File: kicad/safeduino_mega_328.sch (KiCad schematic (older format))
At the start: 75 parts, among them X1 USB

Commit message: Заменил FTDI на Atmega16u2.
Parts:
- removed DD2: FT232RL, symbol FT232RL
- removed DD3: ADUM1201, symbol ADUM1201
- removed XSJG1: ~, ~, symbol PIN_M_4
- added C1: 22п, symbol CAPITORS
- added C10, C8, C9: 0.1мк, symbol CAPITORS
- added DD2: ATMEGA16U2-MU, ~, symbol ATMEGA16U2-MU
- added DD3: ADUM1301, ~, symbol ADUM1301
- added R10, R12, R13: 10к, symbol RESISTOR
- added R11: 1M, symbol RESISTOR
- added R14, R15: 0, symbol RESISTOR
- added R16: 1М, symbol RESISTOR
- added R9: 1к, symbol RESISTOR
- added VD5: BAS216, ~, symbol DIODE
- added XP1: PLD-6, ~, symbol PIN_M_6
- added Z2: 16МГц, symbol QUARTZ_RESONATOR
- C3: value 0.1мк -> 22п
- C5: value 0.1мк -> 1мк
- R3: value 47 -> 22
- R4: value 1к -> 22
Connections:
- net labels added: D+, D-, MISO2, MOSI2, PE0, PE1, RESET2, RESET_16U2, RXI, SCK2, TXI
- net labels removed: CTS, DCD, DSR, RI
- wire segments 237 -> 326
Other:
- note removed: "MISO"
- note removed: "MOSI"
- note removed: "RESET"
- note removed: "SCK"
- moved on the sheet: C13, C14, C15, C16, C17, C18, C2, C21, C23, C6, C7, DA1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

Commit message: Начал переразводить печатную плату.
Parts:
- R14: value 0 -> 1к
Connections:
- wire segments 326 -> 280
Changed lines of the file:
@@
 	13050 9450 13300 9450
 Wire Wire Line
-	4150 3400 4150 4000
-Wire Wire Line
-	4150 4000 4150 4150
+	4150 3400 4150 4150
 Wire Wire Line
 	4150 3400 3700 3400
@@
 	2750 4600 2750 4400
 Wire Wire Line
-	2750 4600 3550 4600
-Wire Wire Line
-	3550 4600 4150 4600
-Wire Wire Line
-	4150 4600 4900 4600
-Wire Wire Line
-	4900 4600 5500 4600
+	2750 4600 5500 4600
 Wire Wire Line
 	1650 1850 1650 1600
@@
 Connection ~ 4150 4000
 Wire Wire Line
-	2200 4000 2750 4000
-Wire Wire Line
-	2750 4000 3100 4000
+	2200 4000 3100 4000
 Wire Wire Line
 	4150 4600 4150 4400
@@
 Connection ~ 12200 2450
 Wire Wire Line
-	10650 2450 12200 2450
-Wire Wire Line
-	12200 2450 12650 2450
+	10650 2450 12650 2450
 Connection ~ 11200 2650
 Wire Wire Line
-	10650 2650 11200 2650
-Wire Wire Line
-	11200 2650 11650 2650
+	10650 2650 11650 2650
 Wire Wire Line
 	11200 3000 11200 3250
@@
 Connection ~ 9400 3950
 Wire Wire Line
-	9250 3950 9400 3950
-Wire Wire Line
-	9400 3950 9650 3950
+	9250 3950 9650 3950
 Wire Wire Line
 	8550 4150 8400 4150
@@
 	14450 1250 14900 1250
 Wire Wire Line
-	14450 1350 14800 1350
-Wire Wire Line
-	14800 1350 14900 1350
+	14450 1350 14900 1350
 Wire Wire Line
 	14450 1150 14900 1150
@@
 	6700 2750 7000 2750
 Wire Wire Line
-	6700 2750 6700 2950
-Wire Wire Line
-	6700 2950 6700 3500
-Wire Wire Line
-	6700 3500 6700 3600
+	6700 2750 6700 3600
 Connection ~ 6450 3950
 Wire Wire Line
@@
 	6600 3500 6700 3500
 Wire Wire Line
-	10750 2850 10750 2950
-Wire Wire Line
-	10750 2950 10750 3050
+	10750 2850 10750 3050
 Wire Wire Line
 	10750 2850 10650 2850
@@
 	6100 2450 7000 2450
 Wire Wire Line
-	2450 2300 2950 2300
-Wire Wire Line
-	2950 2300 3050 2300
-Wire Wire Line
-	1550 7450 1650 7450
-Wire Wire Line
-	1650 7450 2050 7450
+	2450 2300 3050 2300
+Wire Wire Line
+	1550 7450 2050 7450
 Connection ~ 1650 7450
 Wire Wire Line
@@
 	6200 3950 6200 3850
 Wire Wire Line
-	6200 3950 6450 3950
-Wire Wire Line
-	6450 3950 6700 3950
+	6200 3950 6700 3950
 Wire Wire Line
 	6700 3950 6700 3850
@@
 	6200 2650 7000 2650
 Wire Wire Line
-	6200 2650 6200 2950
-Wire Wire Line
-	6200 2950 6200 3500
-Wire Wire Line
-	6200 3500 6200 3600
+	6200 2650 6200 3600
 Wire Wire Line
 	7000 1850 6100 1850
@@
 	6100 2050 7000 2050
 Wire Wire Line
-	8100 3950 8400 3950
-Wire Wire Line
-	8400 3950 8550 3950
+	8100 3950 8550 3950
 Connection ~ 8400 3950
 Wire Wire Line
@@
 	4700 2400 5150 2400
 Wire Wire Line
-	10650 3050 10750 3050
-Wire Wire Line
-	10750 3050 11050 3050
+	10650 3050 11050 3050
 Connection ~ 10750 3050
 Wire Wire Line
@@
 	12200 3400 12200 3650
 Wire Wire Line
-	10650 2550 11700 2550
-Wire Wire Line
-	11700 2550 12150 2550
+	10650 2550 12150 2550
 Connection ~ 11700 2550
 Wire Wire Line
@@
 	12300 6800 13100 6800
 Wire Wire Line
-	4000 4000 4150 4000
-Wire Wire Line
-	4150 4000 4900 4000
-Wire Wire Line
-	4900 4000 5500 4000
+	4000 4000 5500 4000
 Connection ~ 4900 4000
 Wire Wire Line
@@
 	1950 2500 1450 2500
 Wire Wire Line
-	2750 3400 2750 4000
-Wire Wire Line
-	2750 4000 2750 4150
+	2750 3400 2750 4150
 Wire Wire Line
 	2750 3400 3400 3400
@@
 	3400 8800 3700 8800
 Wire Wire Line
-	3400 8800 3400 9000
-Wire Wire Line
-	3400 9000 3400 9550
-Wire Wire Line
-	3400 9550 3400 9650
+	3400 8800 3400 9650
 Connection ~ 3150 10000
 Wire Wire Line
-	3150 10250 3150 10000
+	3150 10450 3150 10000
 Wire Wire Line
 	3300 9550 3400 9550
@@
 	2900 10000 2900 9900
 Wire Wire Line
-	2900 10000 3150 10000
-Wire Wire Line
-	3150 10000 3400 10000
+	2900 10000 3400 10000
 Wire Wire Line
 	3400 10000 3400 9900
@@
 	2900 8700 3700 8700
 Wire Wire Line
-	2900 8700 2900 9000
-Wire Wire Line
-	2900 9000 2900 9550
-Wire Wire Line
-	2900 9550 2900 9650
+	2900 8700 2900 9650
 Wire Wire Line
 	3400 9000 3275 9000
@@
 	1    0    0    -1
 $EndComp
-Text Label 3150 10250 1    60   ~ 0
-GND
 $Comp
 L CAPITORS C3
@@
 	2400 9550 2400 9450
 Wire Wire Line
-	1800 9550 2100 9550
-Wire Wire Line
-	2100 9550 2400 9550
+	1800 9550 2400 9550
 Wire Wire Line
 	1800 9550 1800 9450
@@
 GND_USB
 Wire Wire Line
-	7650 8200 9050 8200
-Wire Wire Line
-	9050 8200 9450 8200
+	7650 8200 9450 8200
 Text Label 9450 8200 2    60   ~ 0
 5V_USB
@@
 	7650 8600 7750 8600
 Wire Wire Line
-	7750 8600 7750 8700
-Wire Wire Line
-	7750 8700 7750 8850
+	7750 8600 7750 8850
 Wire Wire Line
 	7750 8700 7650 8700
 Wire Wire Line
-	7750 8850 7950 8850
-Wire Wire Line
-	7950 8850 8500 8850
-Wire Wire Line
-	8500 8850 9050 8850
+	7750 8850 9050 8850
 Wire Wire Line
 	7950 8850 7950 8750
 Connection ~ 7750 8700
 Wire Wire Line
-	7650 8400 7950 8400
-Wire Wire Line
-	7950 8400 8350 8400
+	7650 8400 8350 8400
 Wire Wire Line
 	7950 8400 7950 8500
@@
 $EndComp
 Wire Wire Line
-	7650 8300 8500 8300
-Wire Wire Line
-	8500 8300 8900 8300
+	7650 8300 8900 8300
 Wire Wire Line
 	8500 8300 8500 8500
@@
 Connection ~ 7950 8400
 Wire Wire Line
-	8500 8750 8500 8850
-Wire Wire Line
-	8500 8850 8500 9300
+	8500 8750 8500 9300
 Connection ~ 7950 8850
 Wire Wire Line
@@
 	1450 5500 2150 5500
 Wire Wire Line
-	1450 5600 2600 5600
-Wire Wire Line
-	2600 5600 2750 5600
+	1450 5600 2750 5600
 Wire Wire Line
 	2050 5700 1450 5700
@@
 	2800 5900 2600 5900
 Wire Wire Line
-	2600 5600 2600 5900
-Wire Wire Line
-	2600 5900 2600 6250
+	2600 5600 2600 6250
 Connection ~ 2600 5600
 Wire Wire Line
-	3050 5600 3200 5600
-Wire Wire Line
-	3200 5600 3600 5600
+	3050 5600 3600 5600
 Wire Wire Line
 	3200 5600 3200 5900
@@
 	9900 6300 9900 6600
 Wire Wire Line
-	9500 6600 9900 6600
-Wire Wire Line
-	9900 6600 10000 6600
+	9500 6600 10000 6600
 Connection ~ 9900 6600
 Text Label 9500 6600 0    60   ~ 0
@@
 	9800 7550 9800 7200
 Wire Wire Line
-	9350 7200 9800 7200
-Wire Wire Line
-	9800 7200 10000 7200
+	9350 7200 10000 7200
 Wire Wire Line
 	10000 7300 9900 7300
@@
 	9900 7300 9900 7400
 Wire Wire Line
-	9350 7400 9900 7400
-Wire Wire Line
-	9900 7400 10000 7400
+	9350 7400 10000 7400
 Text Label 9350 7400 0    60   ~ 0
 GND_USB
@@
 	11900 7300 11900 7400
 Wire Wire Line
-	11800 7400 11900 7400
-Wire Wire Line
-	11900 7400 12550 7400
+	11800 7400 12550 7400
 Connection ~ 11900 7400
 Text Label 12550 7400 2    60   ~ 0
@@
 	12000 7550 12000 7200
 Wire Wire Line
-	11800 7200 12000 7200
-Wire Wire Line
-	12000 7200 12550 7200
+	11800 7200 12550 7200
 Connection ~ 12000 7200
 $Comp
@@
 P 11900 5850
 F 0 "R14" V 12100 6050 71  0000 C CNN
-F 1 "0" V 11950 6050 71  0000 C CNN
+F 1 "1к" V 11950 6050 71  0000 C CNN
 F 2 "" H 11900 5850 60  0001 C CNN
 F 3 "" H 11900 5850 60  0001 C CNN
 	1    11900 5850
-	0    1    -1   0
+	0    -1   -1   0
 $EndComp
 Wire Wire Line
@@
 GND
 Wire Wire Line
-	11900 5850 11900 6000
-Wire Wire Line
-	11900 6000 11900 6150
+	11900 5850 11900 6150
 Wire Wire Line
 	11900 6000 12350 6000
@@
 $EndComp
 Wire Wire Line
-	12600 6000 13000 6000
-Wire Wire Line
-	13000 6000 13400 6000
+	12600 6000 13400 6000
 Wire Wire Line
 	13000 6000 13000 5850
@@
 RESET
 Connection ~ 13000 6000
+Text Label 3150 10450 1    60   ~ 0
+GND_USB
 $EndSCHEMATC

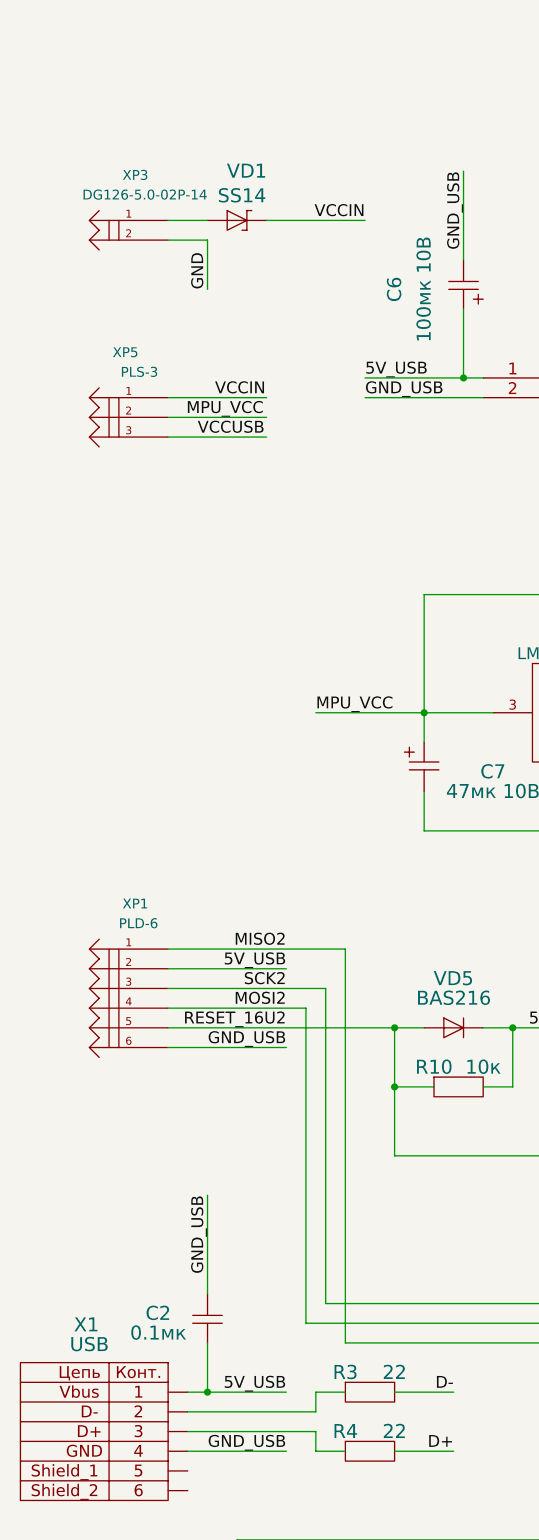
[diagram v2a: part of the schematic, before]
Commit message: Добавил самовостанавливающиеся предохренители на 0.5А.
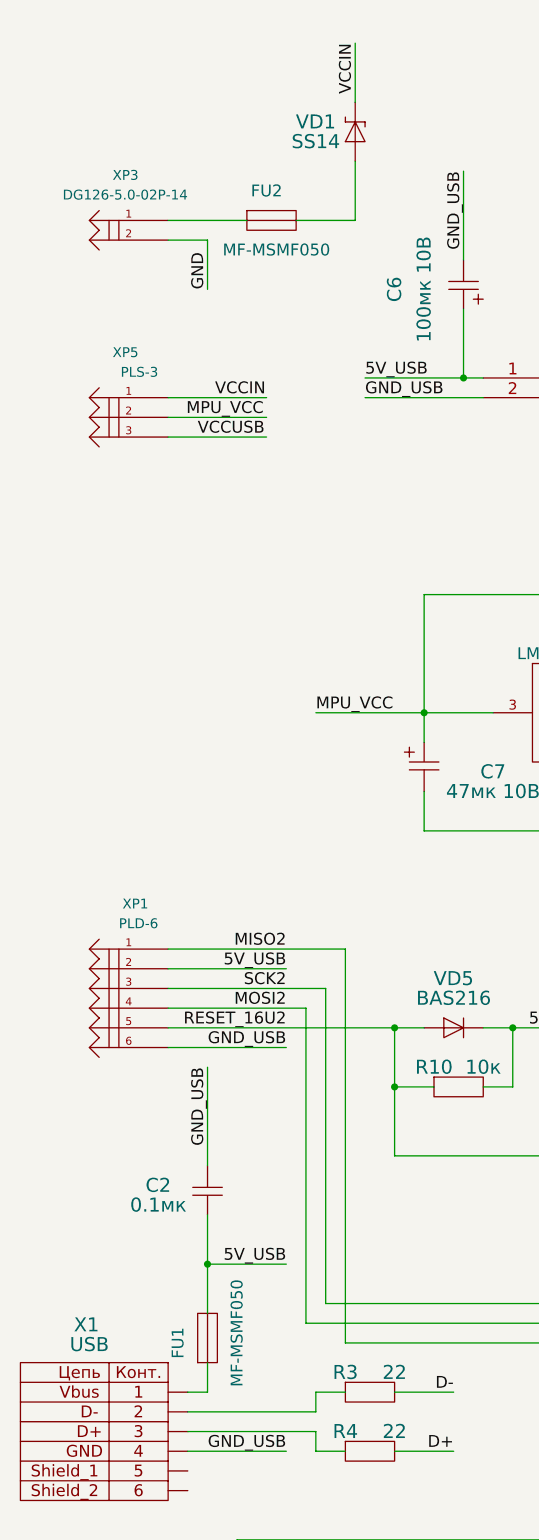
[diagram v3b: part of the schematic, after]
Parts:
- added FU1, FU2: MF-MSMF050, ~, symbol PROTECTOR
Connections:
- wire segments 280 -> 284
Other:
- moved on the sheet: C2, VD1
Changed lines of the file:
@@
 Sheet 1 1
 Title "SafeDuino MEGA 328"
-Date "19 feb 2016"
+Date "24 feb 2016"
 Rev "1.02"
 Comp ""
@@
 	13450 2250 13000 2250
 Wire Wire Line
-	1950 1500 2450 1500
-Wire Wire Line
 	1950 2600 1450 2600
 Wire Wire Line
@@
 	2450 2300 3050 2300
 Wire Wire Line
-	1550 7450 2050 7450
-Connection ~ 1650 7450
-Wire Wire Line
-	1650 7200 1650 7450
-Wire Wire Line
-	1650 6950 1650 6450
+	1650 6800 2050 6800
+Connection ~ 1650 6800
+Wire Wire Line
+	1650 6550 1650 7050
+Wire Wire Line
+	1650 6300 1650 5800
 Wire Wire Line
 	12000 8050 12000 7800
@@
 	14900 1550 14450 1550
 Wire Wire Line
-	1450 1500 1650 1500
+	1450 1500 1850 1500
 Wire Wire Line
 	6700 2950 6575 2950
@@
 L SHOTTKY_DIODE VD1
 U 1 1 4E20581A
-P 1650 1500
-F 0 "VD1" H 1850 1750 71  0000 C CNN
-F 1 "SS14" H 1825 1625 71  0000 C CNN
-F 2 "" H 1650 1500 60  0001 C CNN
-F 3 "" H 1650 1500 60  0001 C CNN
-	1    1650 1500
-	1    0    0    -1
-$EndComp
-Text Label 2450 1500 2    60   ~ 0
+P 2400 1200
+F 0 "VD1" V 2600 1400 71  0000 C CNN
+F 1 "SS14" V 2500 1400 71  0000 C CNN
+F 2 "" H 2400 1200 60  0001 C CNN
+F 3 "" H 2400 1200 60  0001 C CNN
+	1    2400 1200
+	0    -1   -1   0
+$EndComp
+Text Label 2400 600  3    60   ~ 0
 VCCIN
 Text Label 1600 2600 0    60   ~ 0
@@
 U 1 1 4E1EF82E
 P 1450 1500
-F 0 "XP3" H 1550 1700 50  0000 L BNN
-F 1 "DG126-5.0-02P-14" H 1250 1600 50  0000 L BNN
+F 0 "XP3" H 1600 1700 50  0000 L BNN
+F 1 "DG126-5.0-02P-14" H 1350 1600 50  0000 L BNN
 F 2 "~" H 1900 1650 50  0001 C CNN
 F 3 "" H 1450 1500 60  0001 C CNN
@@
 	0    -1   -1   0
 $EndComp
-Text Label 1650 6450 3    60   ~ 0
+Text Label 1650 5800 3    60   ~ 0
 GND_USB
 $Comp
 L CAPITORS C2
 U 1 1 4CE3E694
-P 1650 7200
-F 0 "C2" V 1800 7450 71  0000 C CNN
-F 1 "0.1мк" V 1700 7450 71  0000 C CNN
-F 2 "" H 1650 7200 60  0001 C CNN
-F 3 "" H 1650 7200 60  0001 C CNN
-	1    1650 7200
+P 1650 6550
+F 0 "C2" V 1800 6800 71  0000 C CNN
+F 1 "0.1мк" V 1700 6800 71  0000 C CNN
+F 2 "" H 1650 6550 60  0001 C CNN
+F 3 "" H 1650 6550 60  0001 C CNN
+	1    1650 6550
 	0    -1   -1   0
 $EndComp
-Text Label 2050 7450 2    60   ~ 0
+Text Label 2050 6800 2    60   ~ 0
 5V_USB
 $Comp
@@
 Text Label 3150 10450 1    60   ~ 0
 GND_USB
+$Comp
+L PROTECTOR FU2
+U 1 1 56CDAEE3
+P 1850 1500
+F 0 "FU2" H 1950 1650 60  0000 C CNN
+F 1 "MF-MSMF050" H 2000 1350 60  0000 C CNN
+F 2 "~" H 1850 1500 60  0000 C CNN
+F 3 "~" H 1850 1500 60  0000 C CNN
+	1    1850 1500
+	1    0    0    -1
+$EndComp
+Wire Wire Line
+	2100 1500 2400 1500
+Wire Wire Line
+	2400 1500 2400 1200
+Wire Wire Line
+	2400 900  2400 600
+$Comp
+L PROTECTOR FU1
+U 1 1 56CDB6FF
+P 1650 7300
+F 0 "FU1" H 1750 7450 60  0000 C CNN
+F 1 "MF-MSMF050" H 1800 7150 60  0000 C CNN
+F 2 "~" H 1650 7300 60  0000 C CNN
+F 3 "~" H 1650 7300 60  0000 C CNN
+	1    1650 7300
+	0    -1   -1   0
+$EndComp
+Wire Wire Line
+	1550 7450 1650 7450
+Wire Wire Line
+	1650 7450 1650 7300
 $EndSCHEMATC

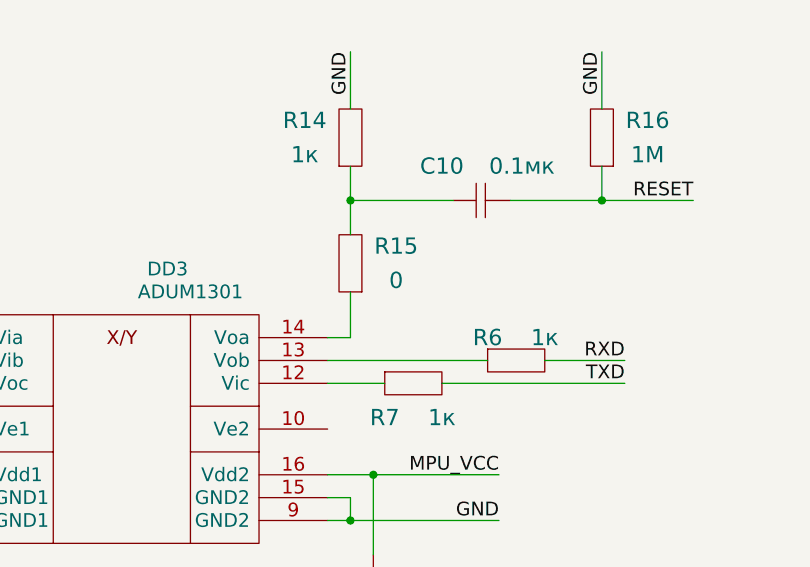
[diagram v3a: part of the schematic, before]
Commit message: Заменил резистор R15 на диод VD6  для защиты ADUM от попадания напряжения.
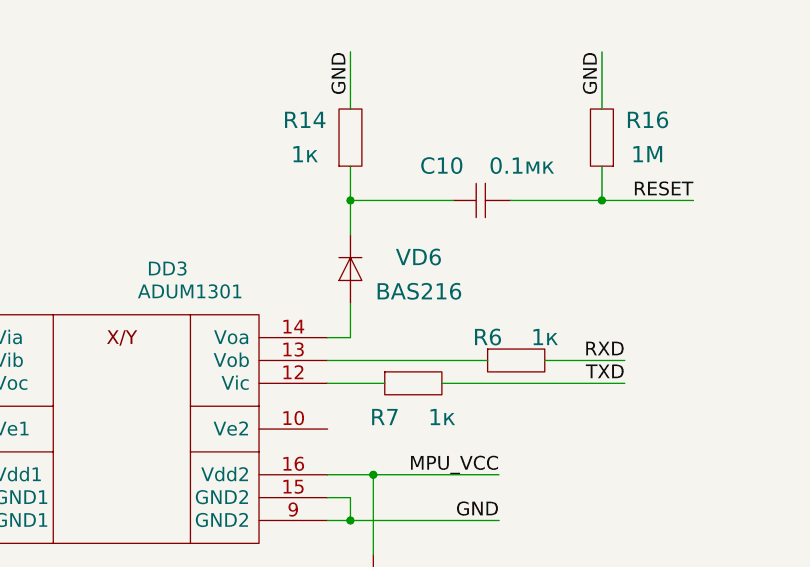
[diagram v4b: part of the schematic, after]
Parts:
- removed R15: 0, symbol RESISTOR
- added VD6: BAS216, ~, symbol DIODE
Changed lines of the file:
@@
 Sheet 1 1
 Title "SafeDuino MEGA 328"
-Date "24 feb 2016"
+Date "10 mar 2016"
 Rev "1.02"
 Comp ""
@@
 	11800 7200 12550 7200
 Connection ~ 12000 7200
-$Comp
-L RESISTOR R15
-U 1 1 56C751AF
-P 11900 6400
-F 0 "R15" V 12100 6600 71  0000 C CNN
-F 1 "0" V 11950 6600 71  0000 C CNN
-F 2 "" H 11900 6400 60  0001 C CNN
-F 3 "" H 11900 6400 60  0001 C CNN
-	1    11900 6400
-	0    1    -1   0
-$EndComp
 Wire Wire Line
 	11800 6600 11900 6600
 Wire Wire Line
-	11900 6600 11900 6400
+	11900 6600 11900 6450
 $Comp
 L RESISTOR R14
@@
 Wire Wire Line
 	1650 7450 1650 7300
+$Comp
+L DIODE VD6
+U 1 1 56E17580
+P 11900 6450
+F 0 "VD6" V 12100 6150 71  0000 C CNN
+F 1 "BAS216" V 11950 6150 71  0000 C CNN
+F 2 "~" H 11900 6450 60  0000 C CNN
+F 3 "~" H 11900 6450 60  0000 C CNN
+	1    11900 6450
+	0    -1   -1   0
+$EndComp
 $EndSCHEMATC

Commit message: SafeDuino MEGA 328 v1.02 полностью готова к отправке на изготовление.
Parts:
- DD1: symbol ATMEGA168-20AU -> ATmega168-20AU
- S1: symbol BUTTON_SMD_1 -> button_smd_1
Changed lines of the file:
@@
 EESchema Schematic File Version 2
+LIBS:safeduino_mega_328-rescue
 LIBS:LFcapitors
 LIBS:LFcomponents
@@
 LIBS:LFtransistor
 LIBS:safeduino_mega_328-cache
-EELAYER 27 0
+EELAYER 25 0
 EELAYER END
 $Descr A3 16535 11693
@@
 RESET
 $Comp
-L BUTTON_SMD_1 S1
+L button_smd_1 S1
 U 1 1 4CE689D3
 P 8550 3950
@@
 5V_USB
 $Comp
-L ATMEGA168-20AU DD1
+L ATmega168-20AU DD1
 U 1 1 4CE2AA57
 P 7300 1050

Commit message: Исправли ошибку на плате SafeDuino MEGA 328(был не соединён контакт PE0 на плате).
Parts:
- R12: value 10к -> 47
- R13: value 10к -> 1к
- R16: value 1М -> 1M
- VT1: symbol NPN -> NPN-RESCUE-safeduino_mega_328
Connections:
- net PE1: now also DD2.8 (PD2(RXD1/AIN1/INT2))
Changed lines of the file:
@@
 $EndComp
 $Comp
-L NPN VT1
+L NPN-RESCUE-safeduino_mega_328 VT1
 U 1 1 4E5E2697
 P 13850 9450
@@
 PE1
 Wire Wire Line
-	3450 8000 3850 8000
+	3450 8000 3700 8000
 Wire Wire Line
 	7650 7700 7900 7700
@@
 U 1 1 56C72CCB
 P 9000 6700
-F 0 "R12" H 8950 6800 71  0000 C CNN
-F 1 "10к" H 9300 6800 71  0000 C CNN
+F 0 "R12" H 9000 6800 71  0000 C CNN
+F 1 "47" H 9250 6800 71  0000 C CNN
 F 2 "" H 9000 6700 60  0001 C CNN
 F 3 "" H 9000 6700 60  0001 C CNN
@@
 P 9900 6300
 F 0 "R13" V 10100 6500 71  0000 C CNN
-F 1 "10к" V 9950 6500 71  0000 C CNN
+F 1 "1к" V 9950 6500 71  0000 C CNN
 F 2 "" H 9900 6300 60  0001 C CNN
 F 3 "" H 9900 6300 60  0001 C CNN
@@
 P 13000 5850
 F 0 "R16" V 13200 6050 71  0000 C CNN
-F 1 "1М" V 13050 6050 71  0000 C CNN
+F 1 "1M" V 13050 6050 71  0000 C CNN
 F 2 "" H 13000 5850 60  0001 C CNN
 F 3 "" H 13000 5850 60  0001 C CNN
